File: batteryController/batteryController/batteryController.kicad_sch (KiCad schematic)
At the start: 15 parts, among them J1 Conn_01x02_Male, J2 Screw_Terminal_01x02, J3 Conn_01x04_Male, J4 Conn_01x04_Male, J5 Conn_01x04_Male, J6 USB_A, U1 ATtiny13V-10P, U2 L7806CV, U3 L78L05_TO92

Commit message: remade basically the entire thing
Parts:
- removed D1: LED, LED_THT:LED_D3.0mm, symbol Device:LED
- removed J1: Conn_01x02_Male, Connector_PinHeader_2.54mm:PinHeader_1x02_P2.54mm_Vertical, symbol Connector:Conn_01x02_Male
- removed J3, J4, J5: Conn_01x04_Male, Connector_PinHeader_2.54mm:PinHeader_1x04_P2.54mm_Vertical, symbol Connector:Conn_01x04_Male
- removed R1: 220, Resistor_THT:R_Axial_DIN0207_L6.3mm_D2.5mm_P7.62mm_Horizontal, symbol Device:R
- removed U3: L78L05_TO92, Package_TO_SOT_THT:TO-92_Inline, symbol Regulator_Linear:L78L05_TO92
- added J1: Conn_02x08_Counter_Clockwise, Connector_PinHeader_2.54mm:PinHeader_2x08_P2.54mm_Vertical, symbol Connector_Generic:Conn_02x08_Counter_Clockwise
- added U3: L78L05_SOT89, Package_TO_SOT_SMD:SOT-89-3, symbol Regulator_Linear:L78L05_SOT89
- R1: renamed from R2; value R -> 2k; footprint Resistor_THT:R_Axial_DIN0207_L6.3mm_D2.5mm_P7.62mm_Horizontal -> Resistor_SMD:R_0603_1608Metric
- R2: renamed from R3; value R -> 680; footprint Resistor_THT:R_Axial_DIN0207_L6.3mm_D2.5mm_P7.62mm_Horizontal -> Resistor_SMD:R_0603_1608Metric
- R3: renamed from R4; value R -> 2k; footprint Resistor_THT:R_Axial_DIN0207_L6.3mm_D2.5mm_P7.62mm_Horizontal -> Resistor_SMD:R_0603_1608Metric
- R4: renamed from R5; value R -> 680; footprint Resistor_THT:R_Axial_DIN0207_L6.3mm_D2.5mm_P7.62mm_Horizontal -> Resistor_SMD:R_0603_1608Metric
- renumbered J6 to J3
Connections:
- net 5V: now also J1.11 (Pin_11), U3.1 (OUT)
- net 6V: now also J1.12 (Pin_12), J1.3 (Pin_3), J1.4 (Pin_4)
- net GND: now also J1.1 (Pin_1), J1.10 (Pin_10), J1.2 (Pin_2), J1.9 (Pin_9), U3.2 (GND)
- net VBUS: now also U3.3 (IN)
- net controll pin: now reaches U1.5 (PB0)
- net controll pin: now also J1.13 (Pin_13)
- net D-: now reaches J3.2 (D-), R3.2, R4.2
- net D+: now reaches J3.3 (D+), R1.2, R2.2
- new net: J1.14 (Pin_14), J1.16 (Pin_16)
- new net: J1.5 (Pin_5), J1.7 (Pin_7)
- new net: J1.6 (Pin_6), J1.8 (Pin_8)
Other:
- moved on the sheet: J2, J3, R1, R2, R3, R4

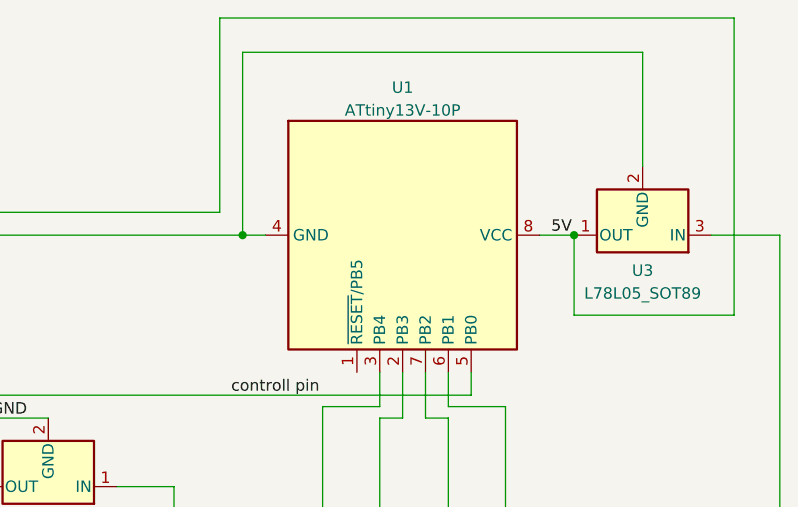
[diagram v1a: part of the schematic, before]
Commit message: fixed DRC warnings
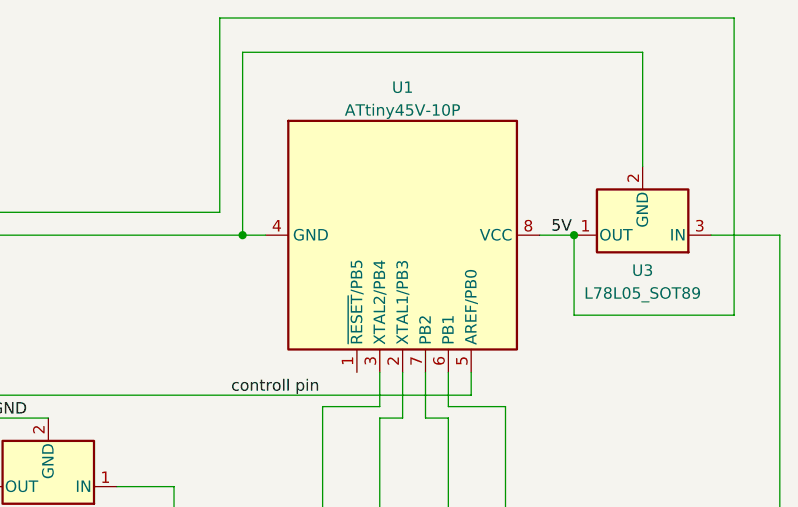
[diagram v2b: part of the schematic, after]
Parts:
- removed U1: ATtiny13V-10P, Package_DIP:DIP-8_W7.62mm, symbol MCU_Microchip_ATtiny:ATtiny13V-10P
- added U1: ATtiny45V-10P, Package_DIP:DIP-8_W7.62mm_Socket, symbol MCU_Microchip_ATtiny:ATtiny45V-10P
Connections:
- net 5V: now also U1.8 (VCC)
- net GND: now also U1.4 (GND)
- net controll pin: now also U1.5 (AREF/PB0)
- net at R2.1: now also U1.2 (XTAL1/PB3)
- net at R1.1: now also U1.3 (XTAL2/PB4)
- net at R4.1: now also U1.6 (PB1)
- net at R3.1: now also U1.7 (PB2)
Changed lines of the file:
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@@
     (effects (font (size 1.27 1.27)) (justify left bottom))
-  )
-  (symbol (lib_id "MCU_Microchip_ATtiny:ATtiny13V-10P") (at 151.13 66.04 270) (unit 1)
-    (in_bom yes) (on_board yes) (fields_autoplaced)
-    (property "Reference" "U1" (id 0) (at 151.13 49.6402 90))
-    (property "Value" "ATtiny13V-10P" (id 1) (at 151.13 52.1771 90))
-    (property "Footprint" "Package_DIP:DIP-8_W7.62mm" (id 2) (at 151.13 66.04 0)
-      (effects (font (size 1.27 1.27) italic) hide)
-    )
-    (property "Datasheet" "http://ww1.microchip.com/downloads/en/DeviceDoc/doc2535.pdf" (id 3) (at 151.13 66.04 0)
-      (effects (font (size 1.27 1.27)) hide)
-    )
-    (pin "1")
-    (pin "2")
-    (pin "3")
-    (pin "4")
-    (pin "5")
-    (pin "6")
-    (pin "7")
-    (pin "8")
   )
   (symbol (lib_id "Regulator_Linear:L78L05_SOT89") (at 177.8 66.04 180) (unit 1)
@@
     (pin "9")
   )
+  (symbol (lib_id "MCU_Microchip_ATtiny:ATtiny45V-10P") (at 151.13 66.04 270) (unit 1)
+    (in_bom yes) (on_board yes) (fields_autoplaced)
+    (property "Reference" "U1" (id 0) (at 151.13 49.6402 90))
+    (property "Value" "ATtiny45V-10P" (id 1) (at 151.13 52.1771 90))
+    (property "Footprint" "Package_DIP:DIP-8_W7.62mm_Socket" (id 2) (at 151.13 66.04 0)
+      (effects (font (size 1.27 1.27) italic) hide)
+    )
+    (property "Datasheet" "http://ww1.microchip.com/downloads/en/DeviceDoc/atmel-2586-avr-8-bit-microcontroller-attiny25-attiny45-attiny85_datasheet.pdf" (id 3) (at 151.13 66.04 0)
+      (effects (font (size 1.27 1.27)) hide)
+    )
+    (pin "1")
+    (pin "2")
+    (pin "3")
+    (pin "4")
+    (pin "5")
+    (pin "6")
+    (pin "7")
+    (pin "8")
+  )
   (symbol (lib_id "Connector:Screw_Terminal_01x02") (at 90.17 114.3 180) (unit 1)
     (in_bom yes) (on_board yes) (fields_autoplaced)
@@
       (reference "R4") (unit 1) (value "680") (footprint "Resistor_SMD:R_0603_1608Metric")
     )
-    (path "/074bd178-4b8d-4443-a5fb-cfcbc87a942c"
-      (reference "U1") (unit 1) (value "ATtiny13V-10P") (footprint "Package_DIP:DIP-8_W7.62mm")
+    (path "/b8b61209-b70d-492d-a05b-6733c40301ab"
+      (reference "U1") (unit 1) (value "ATtiny45V-10P") (footprint "Package_DIP:DIP-8_W7.62mm_Socket")
     )
     (path "/2dc3e3f9-4b13-4051-a201-8af13b42920c"

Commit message: remade it again...
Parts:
- R1, R2, R3, R4: footprint Resistor_SMD:R_0603_1608Metric -> Resistor_SMD:R_0402_1005Metric
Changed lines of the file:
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@@
       (effects (font (size 1.27 1.27)) (justify left))
     )
-    (property "Footprint" "Resistor_SMD:R_0603_1608Metric" (id 2) (at 160.782 100.33 90)
+    (property "Footprint" "Resistor_SMD:R_0402_1005Metric" (id 2) (at 160.782 100.33 90)
       (effects (font (size 1.27 1.27)) hide)
     )
@@
       (effects (font (size 1.27 1.27)) (justify left))
     )
-    (property "Footprint" "Resistor_SMD:R_0603_1608Metric" (id 2) (at 146.812 100.33 90)
+    (property "Footprint" "Resistor_SMD:R_0402_1005Metric" (id 2) (at 146.812 100.33 90)
       (effects (font (size 1.27 1.27)) hide)
     )
@@
       (effects (font (size 1.27 1.27)) (justify left))
     )
-    (property "Footprint" "Resistor_SMD:R_0603_1608Metric" (id 2) (at 140.462 100.33 90)
+    (property "Footprint" "Resistor_SMD:R_0402_1005Metric" (id 2) (at 140.462 100.33 90)
       (effects (font (size 1.27 1.27)) hide)
     )
@@
       (effects (font (size 1.27 1.27)) (justify left))
     )
-    (property "Footprint" "Resistor_SMD:R_0603_1608Metric" (id 2) (at 154.432 100.33 90)
+    (property "Footprint" "Resistor_SMD:R_0402_1005Metric" (id 2) (at 154.432 100.33 90)
       (effects (font (size 1.27 1.27)) hide)
     )
@@
     )
     (path "/efbd3197-cbc9-408a-a2b5-e8292a952aae"
-      (reference "R1") (unit 1) (value "2k") (footprint "Resistor_SMD:R_0603_1608Metric")
+      (reference "R1") (unit 1) (value "2k") (footprint "Resistor_SMD:R_0402_1005Metric")
     )
     (path "/4fd71c9f-fda7-44dc-a730-71f9a293687a"
-      (reference "R2") (unit 1) (value "680") (footprint "Resistor_SMD:R_0603_1608Metric")
+      (reference "R2") (unit 1) (value "680") (footprint "Resistor_SMD:R_0402_1005Metric")
     )
     (path "/f6c853d4-bbcd-4b7b-9a09-2cb0aa558725"
-      (reference "R3") (unit 1) (value "2k") (footprint "Resistor_SMD:R_0603_1608Metric")
+      (reference "R3") (unit 1) (value "2k") (footprint "Resistor_SMD:R_0402_1005Metric")
     )
     (path "/136ccffd-861c-43d7-9c0d-f960a50fef7f"
-      (reference "R4") (unit 1) (value "680") (footprint "Resistor_SMD:R_0603_1608Metric")
+      (reference "R4") (unit 1) (value "680") (footprint "Resistor_SMD:R_0402_1005Metric")
     )
     (path "/b8b61209-b70d-492d-a05b-6733c40301ab"
